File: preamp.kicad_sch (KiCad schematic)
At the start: 13 parts, among them U1 Opamp_Dual

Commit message: add bypass caps to opamps + swap poweramps + layout progress
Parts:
- added C77: 10u, invendelirium_audio:C_0603, symbol Device:C
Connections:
- net GND: now also C77.2
- net vcc_preamp: now also C77.1
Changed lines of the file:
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@@
   (junction (at 72.39 46.99) (diameter 0) (color 0 0 0 0)
   )
+  (junction (at 109.22 100.33) (diameter 0) (color 0 0 0 0)
+  )
   (junction (at 43.18 130.81) (diameter 0) (color 0 0 0 0)
   )
@@
     (stroke (width 0) (type default))
   )
+  (wire (pts (xy 125.73 97.79) (xy 125.73 100.33))
+    (stroke (width 0) (type default))
+  )
   (wire (pts (xy 40.64 72.39) (xy 43.18 72.39))
     (stroke (width 0) (type default))
@@
     (stroke (width 0) (type default))
   )
+  (wire (pts (xy 125.73 100.33) (xy 109.22 100.33))
+    (stroke (width 0) (type default))
+  )
+  (wire (pts (xy 125.73 85.09) (xy 109.22 85.09))
+    (stroke (width 0) (type default))
+  )
   (wire (pts (xy 43.18 130.81) (xy 43.18 138.43))
     (stroke (width 0) (type default))
@@
   )
   (wire (pts (xy 27.94 72.39) (xy 35.56 72.39))
+    (stroke (width 0) (type default))
+  )
+  (wire (pts (xy 125.73 90.17) (xy 125.73 85.09))
     (stroke (width 0) (type default))
   )
@@
         )
       )
+    )
+  )
+  (symbol (lib_id "Device:C") (at 125.73 93.98 0) (unit 1)
+    (in_bom yes) (on_board yes) (dnp no)
+    (property "Reference" "C77" (at 127 91.44 0)
+      (effects (font (size 1.27 1.27)) (justify left))
+    )
+    (property "Value" "10u" (at 127 96.52 0)
+      (effects (font (size 1.27 1.27)) (justify left))
+    )
+    (property "Footprint" "invendelirium_audio:C_0603" (at 126.6952 97.79 0)
+      (effects (font (size 1.27 1.27)) hide)
+    )
+    (property "Datasheet" "~" (at 125.73 93.98 0)
+      (effects (font (size 1.27 1.27)) hide)
+    )
+    (property "Voltage" "16V" (at 125.73 93.98 0)
+      (effects (font (size 1.27 1.27)) hide)
+    )
+    (pin "1")
+    (pin "2")
+    (instances
+      (project "uberamp1"
+        (path "/310059c1-d84b-43e2-9c9a-0e426c534a12/5156a0a1-195e-40e3-846d-487893ba8fa7"
+          (reference "C77") (unit 1)
+        )
+        (path "/310059c1-d84b-43e2-9c9a-0e426c534a12/f0f90934-0ffc-42c4-856c-3b886cd79d06"
+          (reference "C78") (unit 1)
+        )
+        (path "/310059c1-d84b-43e2-9c9a-0e426c534a12/c6ef957f-dbb4-496d-aec2-44492c2243c4"
+          (reference "CU1") (unit 1)
+        )
+        (path "/310059c1-d84b-43e2-9c9a-0e426c534a12/1727f815-1282-4ad8-874c-d1f66f4d7fbe"
+          (reference "CU4") (unit 1)
+        )
+        (path "/310059c1-d84b-43e2-9c9a-0e426c534a12/e09aca01-5377-42b6-85e8-8afbf1155690"
+          (reference "CU5") (unit 1)
+        )
+        (path "/310059c1-d84b-43e2-9c9a-0e426c534a12/b23c2595-3b45-43cf-b3fd-b0c94e6d7f84"
+          (reference "CU6") (unit 1)
+        )
+      )

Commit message: route 1 preamp
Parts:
- added s0, s1: sum0, TestPoint:TestPoint_Pad_D1.5mm, symbol Connector:TestPoint
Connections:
- net ~out0: now also U1.1; no longer U1.7
- net ~out1: now also U1.7; no longer U1.1
- net at R3.2, R4.2, R5.2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: now also U1.6 (-), s0.1; no longer U1.2 (-)
- net at R1.2, R2.1, R76.2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: now also U1.2 (-), s1.1; no longer U1.6 (-)
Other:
- moved on the sheet: U1A, U1B
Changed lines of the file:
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@@
 (kicad_sch (version 20230121) (generator eeschema)
   (paper "A4")
+  (junction (at 44.45 49.53) (diameter 0) (color 0 0 0 0)
+  )
+  (junction (at 44.45 107.95) (diameter 0) (color 0 0 0 0)
+  )
   (junction (at 27.94 72.39) (diameter 0) (color 0 0 0 0)
   )
@@
   (junction (at 43.18 115.57) (diameter 0) (color 0 0 0 0)
   )
+  (junction (at 50.8 49.53) (diameter 0) (color 0 0 0 0)
+  )
   (junction (at 25.4 80.01) (diameter 0) (color 0 0 0 0)
   )
   (junction (at 33.02 57.15) (diameter 0) (color 0 0 0 0)
   )
-  (junction (at 50.8 49.53) (diameter 0) (color 0 0 0 0)
-  )
   (junction (at 43.18 49.53) (diameter 0) (color 0 0 0 0)
   )
@@
   (junction (at 43.18 64.77) (diameter 0) (color 0 0 0 0)
   )
-  (wire (pts (xy 43.18 49.53) (xy 50.8 49.53))
+  (wire (pts (xy 43.18 49.53) (xy 44.45 49.53))
     (stroke (width 0) (type default))
   )
@@
     (stroke (width 0) (type default))
   )
+  (wire (pts (xy 44.45 107.95) (xy 49.53 107.95))
+    (stroke (width 0) (type default))
+  )
   (wire (pts (xy 73.66 116.84) (xy 73.66 105.41))
     (stroke (width 0) (type default))
@@
     (stroke (width 0) (type default))
   )
+  (wire (pts (xy 44.45 49.53) (xy 50.8 49.53))
+    (stroke (width 0) (type default))
+  )
   (wire (pts (xy 40.64 49.53) (xy 43.18 49.53))
     (stroke (width 0) (type default))
@@
     (stroke (width 0) (type default))
   )
-  (wire (pts (xy 43.18 107.95) (xy 49.53 107.95))
+  (wire (pts (xy 43.18 107.95) (xy 44.45 107.95))
     (stroke (width 0) (type default))
   )
@@
     )
   )
-  (symbol (lib_id "Device:Opamp_Dual") (at 58.42 105.41 0) (unit 2)
+  (symbol (lib_id "Device:Opamp_Dual") (at 58.42 46.99 0) (unit 2)
     (in_bom yes) (on_board yes) (dnp no) (fields_autoplaced)
-    (property "Reference" "U1" (at 58.42 96.52 0)
-      (effects (font (size 1.27 1.27)))
-    )
-    (property "Value" "Opamp_Dual" (at 58.42 99.06 0)
-      (effects (font (size 1.27 1.27)))
-    )
-    (property "Footprint" "invendelirium_audio:SOIC-8" (at 58.42 105.41 0)
-      (effects (font (size 1.27 1.27)) hide)
-    )
-    (property "Datasheet" "~" (at 58.42 105.41 0)
+    (property "Reference" "U1" (at 58.42 38.1 0)
+      (effects (font (size 1.27 1.27)))
+    )
+    (property "Value" "Opamp_Dual" (at 58.42 40.64 0)
+      (effects (font (size 1.27 1.27)))
+    )
+    (property "Footprint" "invendelirium_audio:SOIC-8" (at 58.42 46.99 0)
+      (effects (font (size 1.27 1.27)) hide)
+    )
+    (property "Datasheet" "~" (at 58.42 46.99 0)
       (effects (font (size 1.27 1.27)) hide)
     )
@@
     )
   )
+  (symbol (lib_id "Connector:TestPoint") (at 44.45 107.95 0) (unit 1)
+    (in_bom yes) (on_board yes) (dnp no)
+    (property "Reference" "s1" (at 43.18 102.87 0)
+      (effects (font (size 1.27 1.27)) (justify left))
+    )
+    (property "Value" "sum0" (at 46.99 106.553 0)
+      (effects (font (size 1.27 1.27)) (justify left) hide)
+    )
+    (property "Footprint" "TestPoint:TestPoint_Pad_D1.5mm" (at 49.53 107.95 0)
+      (effects (font (size 1.27 1.27)) hide)
+    )
+    (property "Datasheet" "~" (at 49.53 107.95 0)
+      (effects (font (size 1.27 1.27)) hide)
+    )
+    (pin "1")
+    (instances
+      (project "uberamp1"
+        (path "/310059c1-d84b-43e2-9c9a-0e426c534a12/c6ef957f-dbb4-496d-aec2-44492c2243c4"
+          (reference "s1") (unit 1)
+        )
+        (path "/310059c1-d84b-43e2-9c9a-0e426c534a12/1727f815-1282-4ad8-874c-d1f66f4d7fbe"
+          (reference "s3") (unit 1)
+        )
+        (path "/310059c1-d84b-43e2-9c9a-0e426c534a12/e09aca01-5377-42b6-85e8-8afbf1155690"
+          (reference "s5") (unit 1)
+        )
+        (path "/310059c1-d84b-43e2-9c9a-0e426c534a12/b23c2595-3b45-43cf-b3fd-b0c94e6d7f84"
+          (reference "s7") (unit 1)
+        )
+      )
+    )
+  )
   (symbol (lib_id "Device:R_Small") (at 58.42 58.42 90) (unit 1)
     (in_bom yes) (on_board yes) (dnp no) (fields_autoplaced)
@@
     )
   )
-  (symbol (lib_id "Device:Opamp_Dual") (at 58.42 46.99 0) (unit 1)
+  (symbol (lib_id "Device:Opamp_Dual") (at 58.42 105.41 0) (unit 1)
     (in_bom yes) (on_board yes) (dnp no) (fields_autoplaced)
-    (property "Reference" "U1" (at 58.42 38.1 0)
-      (effects (font (size 1.27 1.27)))
-    )
-    (property "Value" "Opamp_Dual" (at 58.42 40.64 0)
-      (effects (font (size 1.27 1.27)))
-    )
-    (property "Footprint" "invendelirium_audio:SOIC-8" (at 58.42 46.99 0)
-      (effects (font (size 1.27 1.27)) hide)
-    )
-    (property "Datasheet" "~" (at 58.42 46.99 0)
+    (property "Reference" "U1" (at 58.42 96.52 0)
+      (effects (font (size 1.27 1.27)))
+    )
+    (property "Value" "Opamp_Dual" (at 58.42 99.06 0)
+      (effects (font (size 1.27 1.27)))
+    )
+    (property "Footprint" "invendelirium_audio:SOIC-8" (at 58.42 105.41 0)
+      (effects (font (size 1.27 1.27)) hide)
+    )
+    (property "Datasheet" "~" (at 58.42 105.41 0)
       (effects (font (size 1.27 1.27)) hide)
     )
@@
         )
       )
+    )
+  )
+  (symbol (lib_id "Connector:TestPoint") (at 44.45 49.53 0) (unit 1)
+    (in_bom yes) (on_board yes) (dnp no)
+    (property "Reference" "s0" (at 43.18 44.45 0)
+      (effects (font (size 1.27 1.27)) (justify left))
+    )
+    (property "Value" "sum0" (at 46.99 48.133 0)
+      (effects (font (size 1.27 1.27)) (justify left) hide)
+    )
+    (property "Footprint" "TestPoint:TestPoint_Pad_D1.5mm" (at 49.53 49.53 0)
+      (effects (font (size 1.27 1.27)) hide)
+    )
+    (property "Datasheet" "~" (at 49.53 49.53 0)
+      (effects (font (size 1.27 1.27)) hide)
+    )
+    (pin "1")
+    (instances
+      (project "uberamp1"
+        (path "/310059c1-d84b-43e2-9c9a-0e426c534a12/c6ef957f-dbb4-496d-aec2-44492c2243c4"
+          (reference "s0") (unit 1)
+        )
+        (path "/310059c1-d84b-43e2-9c9a-0e426c534a12/1727f815-1282-4ad8-874c-d1f66f4d7fbe"
+          (reference "s2") (unit 1)
+        )
+        (path "/310059c1-d84b-43e2-9c9a-0e426c534a12/e09aca01-5377-42b6-85e8-8afbf1155690"
+          (reference "s4") (unit 1)
+        )
+        (path "/310059c1-d84b-43e2-9c9a-0e426c534a12/b23c2595-3b45-43cf-b3fd-b0c94e6d7f84"
+          (reference "s6") (unit 1)
+        )
+      )

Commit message: add bypass caps to fakegnd
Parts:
- added C77: 10u, invendelirium_audio:C_0603, symbol Device:C
- renumbered s1 to s0, s0 to s1
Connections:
- net GND: now also C77.2
- net fakegnd: now also C77.1
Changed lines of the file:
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@@
   (junction (at 30.48 64.77) (diameter 0) (color 0 0 0 0)
   )
+  (junction (at 48.26 74.93) (diameter 0) (color 0 0 0 0)
+  )
   (junction (at 49.53 107.95) (diameter 0) (color 0 0 0 0)
   )
@@
     (stroke (width 0) (type default))
   )
-  (wire (pts (xy 48.26 44.45) (xy 48.26 102.87))
+  (wire (pts (xy 48.26 44.45) (xy 48.26 74.93))
     (stroke (width 0) (type default))
   )
@@
     (stroke (width 0) (type default))
   )
+  (wire (pts (xy 48.26 74.93) (xy 48.26 102.87))
+    (stroke (width 0) (type default))
+  )
   (wire (pts (xy 24.13 57.15) (xy 33.02 57.15))
     (stroke (width 0) (type default))
@@
   )
   (wire (pts (xy 43.18 107.95) (xy 44.45 107.95))
+    (stroke (width 0) (type default))
+  )
+  (wire (pts (xy 48.26 74.93) (xy 53.34 74.93))
     (stroke (width 0) (type default))
   )
@@
     )
   )
+  (symbol (lib_id "Device:C") (at 53.34 78.74 0) (unit 1)
+    (in_bom yes) (on_board yes) (dnp no)
+    (property "Reference" "C77" (at 54.61 76.2 0)
+      (effects (font (size 1.27 1.27)) (justify left))
+    )
+    (property "Value" "10u" (at 54.61 81.28 0)
+      (effects (font (size 1.27 1.27)) (justify left))
+    )
+    (property "Footprint" "invendelirium_audio:C_0603" (at 54.3052 82.55 0)
+      (effects (font (size 1.27 1.27)) hide)
+    )
+    (property "Datasheet" "~" (at 53.34 78.74 0)
+      (effects (font (size 1.27 1.27)) hide)
+    )
+    (property "Voltage" "16V" (at 53.34 78.74 0)
+      (effects (font (size 1.27 1.27)) hide)
+    )
+    (pin "1")
+    (pin "2")
+    (instances
+      (project "uberamp1"
+        (path "/310059c1-d84b-43e2-9c9a-0e426c534a12/5156a0a1-195e-40e3-846d-487893ba8fa7"
+          (reference "C77") (unit 1)
+        )
+        (path "/310059c1-d84b-43e2-9c9a-0e426c534a12/f0f90934-0ffc-42c4-856c-3b886cd79d06"
+          (reference "C78") (unit 1)
+        )
+        (path "/310059c1-d84b-43e2-9c9a-0e426c534a12/c6ef957f-dbb4-496d-aec2-44492c2243c4"
+          (reference "CRP0") (unit 1)
+        )
+        (path "/310059c1-d84b-43e2-9c9a-0e426c534a12/1727f815-1282-4ad8-874c-d1f66f4d7fbe"
+          (reference "CRP1") (unit 1)
+        )
+        (path "/310059c1-d84b-43e2-9c9a-0e426c534a12/e09aca01-5377-42b6-85e8-8afbf1155690"
+          (reference "CRP2") (unit 1)
+        )
+        (path "/310059c1-d84b-43e2-9c9a-0e426c534a12/b23c2595-3b45-43cf-b3fd-b0c94e6d7f84"
+          (reference "CRP3") (unit 1)
+        )
+      )
+    )
+  )
   (symbol (lib_id "Device:R_Small") (at 38.1 49.53 90) (unit 1)
     (in_bom yes) (on_board yes) (dnp no) (fields_autoplaced)
@@
   (symbol (lib_id "Connector:TestPoint") (at 44.45 107.95 0) (unit 1)
     (in_bom yes) (on_board yes) (dnp no)
-    (property "Reference" "s1" (at 43.18 102.87 0)
+    (property "Reference" "s0" (at 43.18 102.87 0)
       (effects (font (size 1.27 1.27)) (justify left))
     )
@@
       (project "uberamp1"
         (path "/310059c1-d84b-43e2-9c9a-0e426c534a12/c6ef957f-dbb4-496d-aec2-44492c2243c4"
-          (reference "s1") (unit 1)
-        )
-        (path "/310059c1-d84b-43e2-9c9a-0e426c534a12/1727f815-1282-4ad8-874c-d1f66f4d7fbe"
-          (reference "s3") (unit 1)
-        )
-        (path "/310059c1-d84b-43e2-9c9a-0e426c534a12/e09aca01-5377-42b6-85e8-8afbf1155690"
-          (reference "s5") (unit 1)
-        )
-        (path "/310059c1-d84b-43e2-9c9a-0e426c534a12/b23c2595-3b45-43cf-b3fd-b0c94e6d7f84"
-          (reference "s7") (unit 1)
+          (reference "s0") (unit 1)
+        )
+        (path "/310059c1-d84b-43e2-9c9a-0e426c534a12/1727f815-1282-4ad8-874c-d1f66f4d7fbe"
+          (reference "s2") (unit 1)
+        )
+        (path "/310059c1-d84b-43e2-9c9a-0e426c534a12/e09aca01-5377-42b6-85e8-8afbf1155690"
+          (reference "s4") (unit 1)
+        )
+        (path "/310059c1-d84b-43e2-9c9a-0e426c534a12/b23c2595-3b45-43cf-b3fd-b0c94e6d7f84"
+          (reference "s6") (unit 1)
         )
       )
@@
   (symbol (lib_id "Connector:TestPoint") (at 44.45 49.53 0) (unit 1)
     (in_bom yes) (on_board yes) (dnp no)
-    (property "Reference" "s0" (at 43.18 44.45 0)
+    (property "Reference" "s1" (at 43.18 44.45 0)
       (effects (font (size 1.27 1.27)) (justify left))
     )
@@
       (project "uberamp1"
         (path "/310059c1-d84b-43e2-9c9a-0e426c534a12/c6ef957f-dbb4-496d-aec2-44492c2243c4"
-          (reference "s0") (unit 1)
-        )
-        (path "/310059c1-d84b-43e2-9c9a-0e426c534a12/1727f815-1282-4ad8-874c-d1f66f4d7fbe"
-          (reference "s2") (unit 1)
-        )
-        (path "/310059c1-d84b-43e2-9c9a-0e426c534a12/e09aca01-5377-42b6-85e8-8afbf1155690"
-          (reference "s4") (unit 1)
-        )
-        (path "/310059c1-d84b-43e2-9c9a-0e426c534a12/b23c2595-3b45-43cf-b3fd-b0c94e6d7f84"
-          (reference "s6") (unit 1)
+          (reference "s1") (unit 1)
+        )
+        (path "/310059c1-d84b-43e2-9c9a-0e426c534a12/1727f815-1282-4ad8-874c-d1f66f4d7fbe"
+          (reference "s3") (unit 1)
+        )
+        (path "/310059c1-d84b-43e2-9c9a-0e426c534a12/e09aca01-5377-42b6-85e8-8afbf1155690"
+          (reference "s5") (unit 1)
+        )
+        (path "/310059c1-d84b-43e2-9c9a-0e426c534a12/b23c2595-3b45-43cf-b3fd-b0c94e6d7f84"
+          (reference "s7") (unit 1)
         )
       )
@@
         )
       )
+    )
+  )
+  (symbol (lib_id "power:GND") (at 53.34 82.55 0) (unit 1)
+    (in_bom yes) (on_board yes) (dnp no) (fields_autoplaced)
+    (property "Reference" "#PWR078" (at 53.34 88.9 0)
+      (effects (font (size 1.27 1.27)) hide)
+    )
+    (property "Value" "GND" (at 53.34 87.63 0)
+      (effects (font (size 1.27 1.27)))
+    )
+    (property "Footprint" "" (at 53.34 82.55 0)
+      (effects (font (size 1.27 1.27)) hide)
+    )
+    (property "Datasheet" "" (at 53.34 82.55 0)
+      (effects (font (size 1.27 1.27)) hide)
+    )
+    (pin "1")
+    (instances
+      (project "uberamp1"
+        (path "/310059c1-d84b-43e2-9c9a-0e426c534a12/c6ef957f-dbb4-496d-aec2-44492c2243c4"
+          (reference "#PWR078") (unit 1)
+        )
+        (path "/310059c1-d84b-43e2-9c9a-0e426c534a12/1727f815-1282-4ad8-874c-d1f66f4d7fbe"
+          (reference "#PWR079") (unit 1)
+        )
+        (path "/310059c1-d84b-43e2-9c9a-0e426c534a12/e09aca01-5377-42b6-85e8-8afbf1155690"
+          (reference "#PWR080") (unit 1)
+        )
+        (path "/310059c1-d84b-43e2-9c9a-0e426c534a12/b23c2595-3b45-43cf-b3fd-b0c94e6d7f84"
+          (reference "#PWR081") (unit 1)
+        )
+      )

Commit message: minor schematic updates
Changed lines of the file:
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@@
     )
     (property "Value" "GND" (at 109.22 105.41 0)
-      (effects (font (size 1.27 1.27)))
+      (effects (font (size 1.27 1.27)) hide)
     )
     (property "Footprint" "" (at 109.22 100.33 0)

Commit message: update to kicad 8
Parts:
- renumbered C77 to CRP0, C77 to CU1

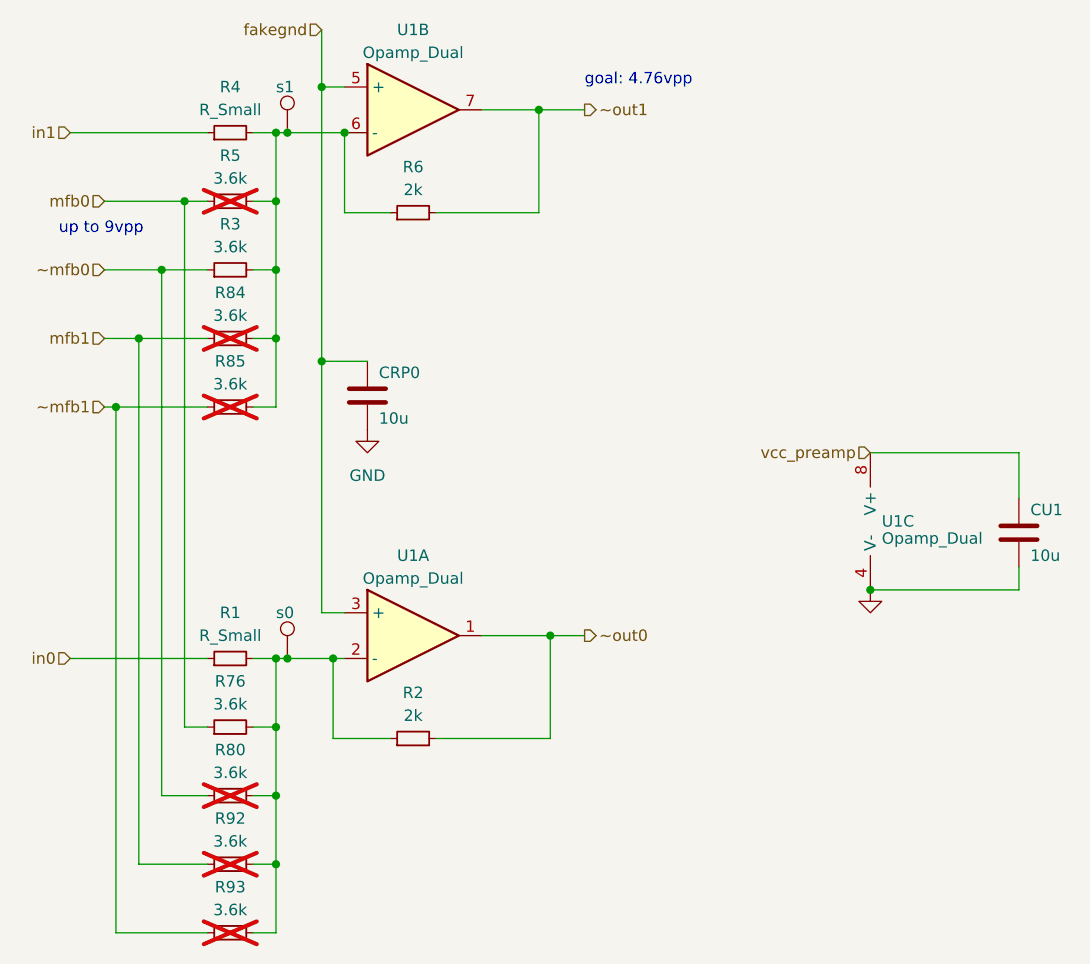
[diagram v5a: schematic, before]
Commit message: add power input +...
+ tons of fixes, footprint assignments, etc
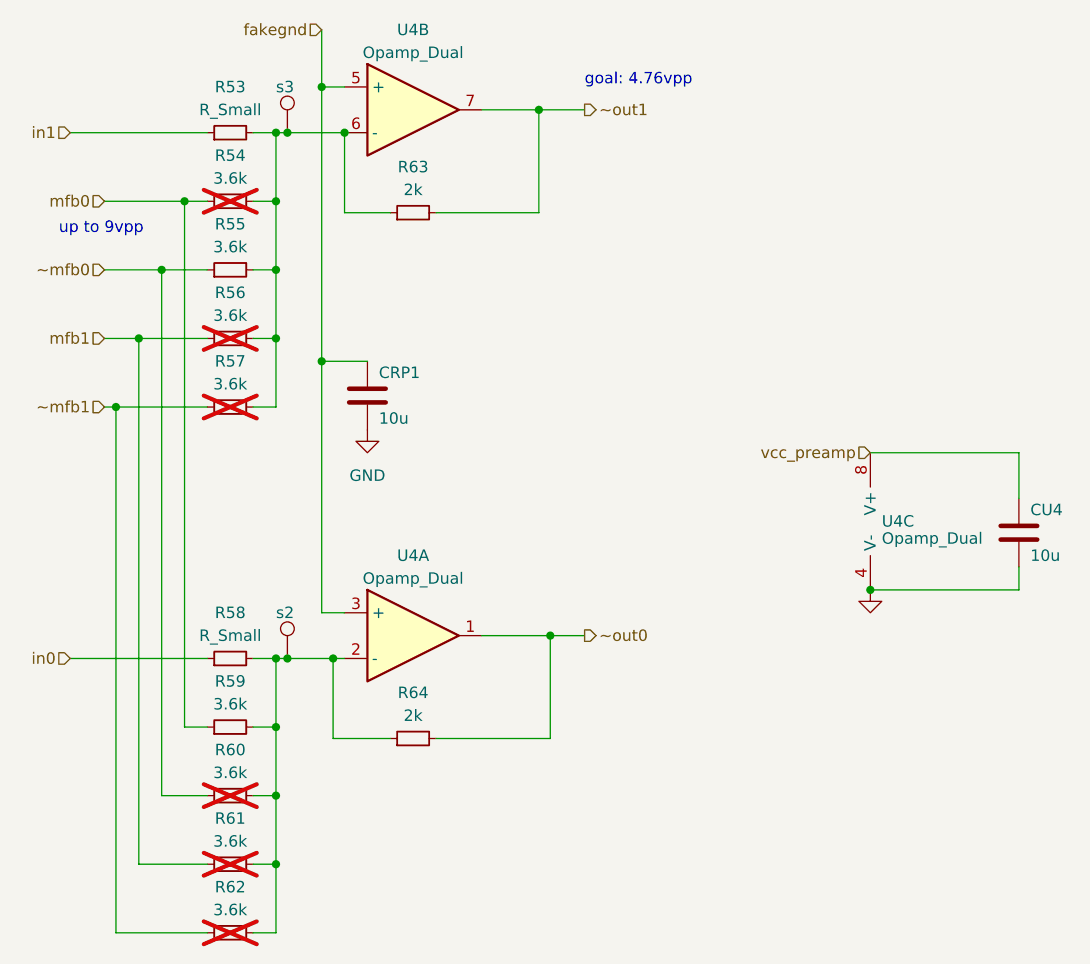
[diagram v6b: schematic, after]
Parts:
- renumbered CRP0 to CRP1, CU1 to CU4, R4 to R53, R5 to R54, R3 to R55, R84 to R56, R85 to R57, R1 to R58, R76 to R59, R80 to R60, R92 to R61, R93 to R62, R6 to R63, R2 to R64, U1 to U4, s0 to s2, s1 to s3
